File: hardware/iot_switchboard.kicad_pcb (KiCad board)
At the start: 2 copper layers, 14 parts, among them IC1 ATTINY44A-SS, P1 CONN_01X05, P2 AVR_ISP

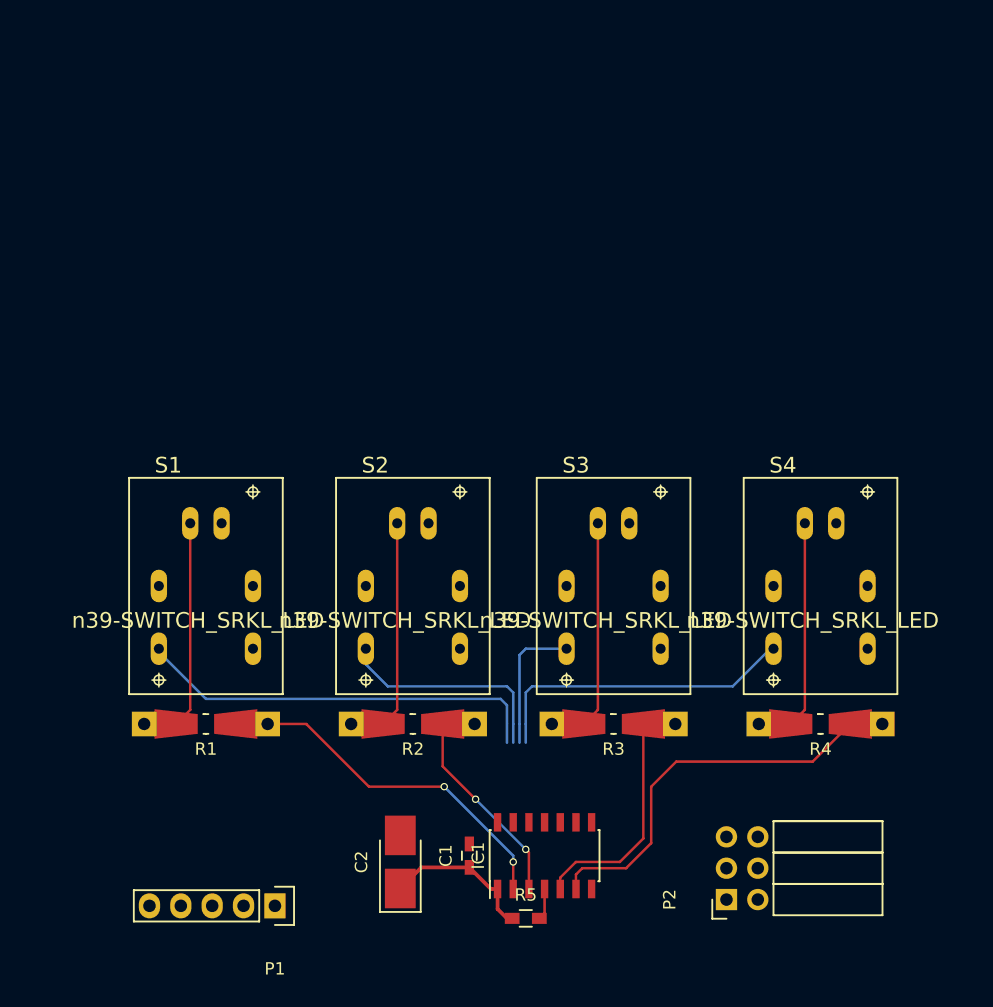
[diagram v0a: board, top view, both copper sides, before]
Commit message: layout and attiny in QFN20
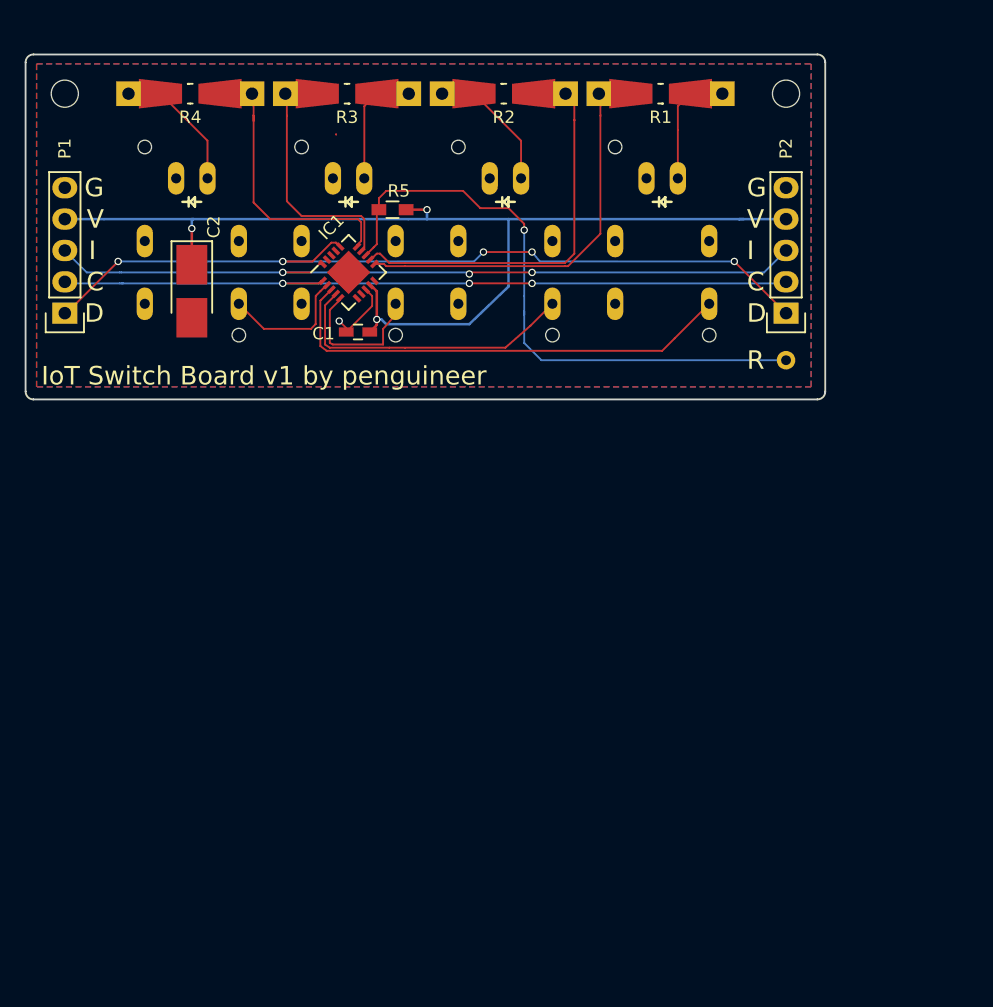
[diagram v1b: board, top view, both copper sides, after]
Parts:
- added REF**: MountingHole_2.2mm_M2_ISO14580, Mounting_Holes:MountingHole_2.2mm_M2_ISO14580, F.Cu at (163.3, 54.6)
- added REF**: MountingHole_2.2mm_M2_ISO14580, Mounting_Holes:MountingHole_2.2mm_M2_ISO14580, F.Cu at (221.7, 54.6)
- added T1: CONN_01X01, Measurement_Points:Measurement_Point_Round-TH_Small, F.Cu at (221.7, 76.2)
- IC1: value ATTINY44A-SS -> ATTINY84-M; footprint Housings_SOIC:SOIC-14_3.9x8.7mm_Pitch1.27mm -> Housings_DFN_QFN:QFN-20-1EP_4x4mm_Pitch0.5mm
- P2: value AVR_ISP -> CONN_01X05; footprint Socket_Strips:Socket_Strip_Angled_2x03 -> Socket_Strips:Socket_Strip_Straight_1x05
- R5: value R -> 10K
- S1, S2, S3, S4: moved to B.Cu
- moved R4 72.2 mm to (173.5, 54.6)
- moved R1 63.0 mm to (211.6, 54.6), turned to 180 degrees
- moved R5 58.4 mm to (189.9, 64.0), turned to 180 degrees
- moved S4 58.1 mm to (173.6, 66.5), turned to 180 degrees
- moved R3 55.4 mm to (186.2, 54.6), turned to 180 degrees
- moved R2 51.6 mm to (198.9, 54.6)
- moved P1 50.9 mm to (163.3, 72.4), turned to 90 degrees
- moved IC1 49.8 mm to (186.3, 69.1), turned to 45 degrees
- moved C2 49.2 mm to (173.6, 70.6), turned to 270 degrees
- moved P2 47.7 mm to (221.7, 72.4)
- moved S1 46.3 mm to (211.7, 66.5), turned to 180 degrees
- moved C1 43.4 mm to (187.1, 73.9), turned to 180 degrees
- moved S3 35.2 mm to (186.3, 66.5), turned to 180 degrees
- moved S2 28.9 mm to (199.0, 66.5), turned to 180 degrees
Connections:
- IC1 pad 1: VCC_IN -> SCL
- IC1 pad 10: SW4 -> (no net)
- IC1 pad 11: SW3 -> LED1
- IC1 pad 12: SW2 -> LED2
- IC1 pad 13: SW1 -> RST
- IC1 pad 14: GND -> LED3
- IC1 pad 2: LED1 -> SW4
- IC1 pad 3: LED2 -> SW1
- IC1 pad 4: RST -> SW2
- IC1 pad 5: LED3 -> SW3
- IC1 pad 6: LED4 -> (no net)
- IC1 pad 7: MOSI -> (no net)
- IC1 pad 8: INT -> GND
- IC1 pad 9: SCK -> VCC_IN
- P1 pad 1: MOSI -> SDA
- P1 pad 2: SCK -> SCL
- P2 pad 1: INT -> SDA
- P2 pad 2: VCC_IN -> SCL
- P2 pad 3: SCK -> INT
- P2 pad 4: MOSI -> VCC_IN
- P2 pad 5: RST -> GND
- S1 pad 4: (no net) -> GND
- S2 pad 4: (no net) -> GND
- S3 pad 4: (no net) -> GND
- S4 pad 4: (no net) -> GND
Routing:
- net VCC_IN: track 12.4 -> 87.1 mm, vias 0 -> 3
- net SDA: track 0.00 -> 68.0 mm, vias 0 -> 5
- net INT: track 0.00 -> 63.8 mm, vias 0 -> 3
- net SCL: track 0.00 -> 62.2 mm, vias 0 -> 3
- net RST: track 2.56 -> 49.9 mm, vias 0 -> 1
- net SW4: track 25.6 -> 10.8 mm
- net LED2: track 18.8 -> 33.3 mm, vias 2 -> 0
- net LED4: track 35.7 -> 23.4 mm
- net Net-(R3-Pad1): track 19.3 -> 9.87 mm
- net Net-(R1-Pad1): track 19.3 -> 9.87 mm
- net Net-(R2-Pad1): track 19.3 -> 11.0 mm
- net Net-(R4-Pad1): track 19.3 -> 11.0 mm
- net GND: track 0.00 -> 5.64 mm, vias 0 -> 1
- net SW2: track 19.0 -> 24.6 mm
- net SW1: track 33.6 -> 38.2 mm
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- added copper zone on B.Cu, net GND
- added copper zone on F.Cu, net GND
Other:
- board outline added: 64.8 x 27.9 mm
- net class DATA: clearance 0.2 -> 0.09906; trace_width 0.2032 -> 0.1524
- net class Default: clearance 0.2 -> 0.1016; trace_width 0.25 -> 0.1524
- net class PWR: clearance 0.2 -> 0.1016; trace_width 0.3048 -> 0.2032
- rule trace_clearance: 0.2 -> 0.1016
- rule trace_min: 0.2 -> 0.1
- rule via_min_drill: 0.3 -> 0.2
- rule via_min_size: 0.4 -> 0.3
- board text added: "C"
- board text added: "D"
- board text added: "G"
- board text added: "I"
- board text added: "IoT Switch Board v1 by penguineer"
- board text added: "R"
- board text added: "V"

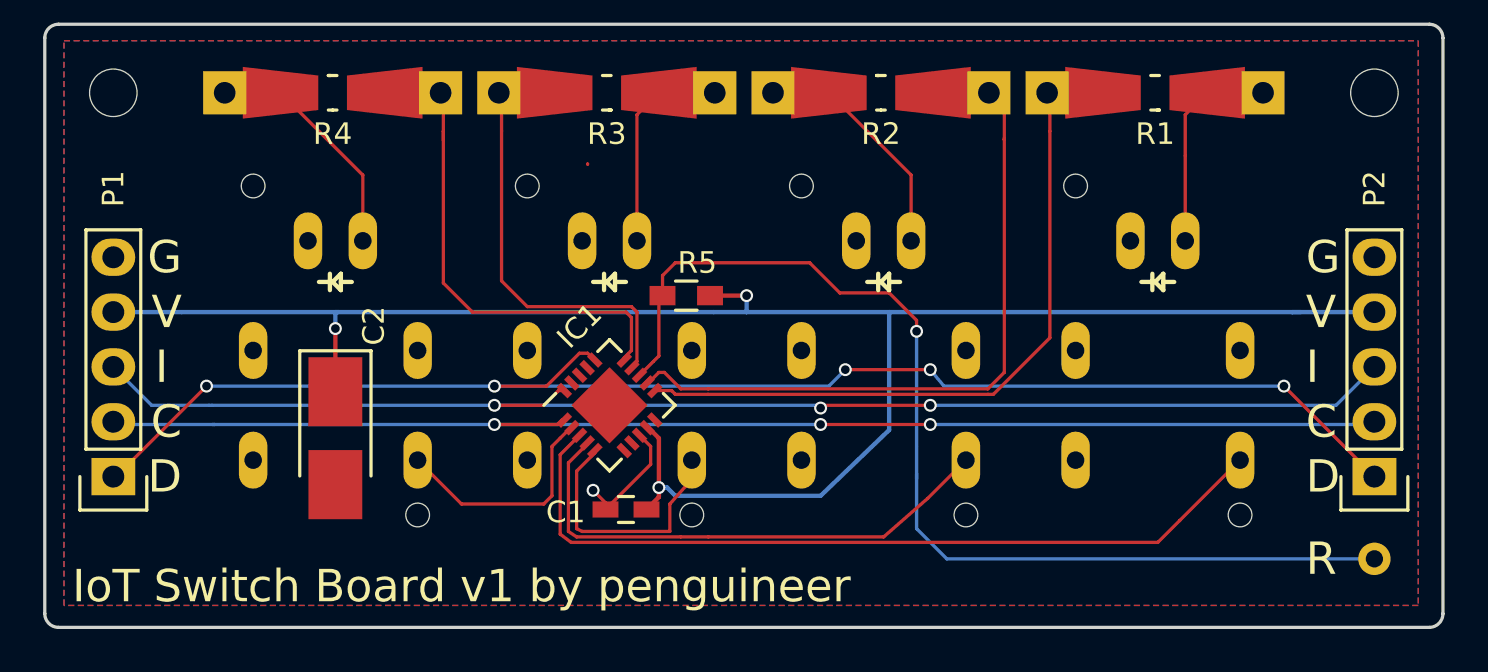
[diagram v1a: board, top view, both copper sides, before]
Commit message: Adapt to Oshpark design rules
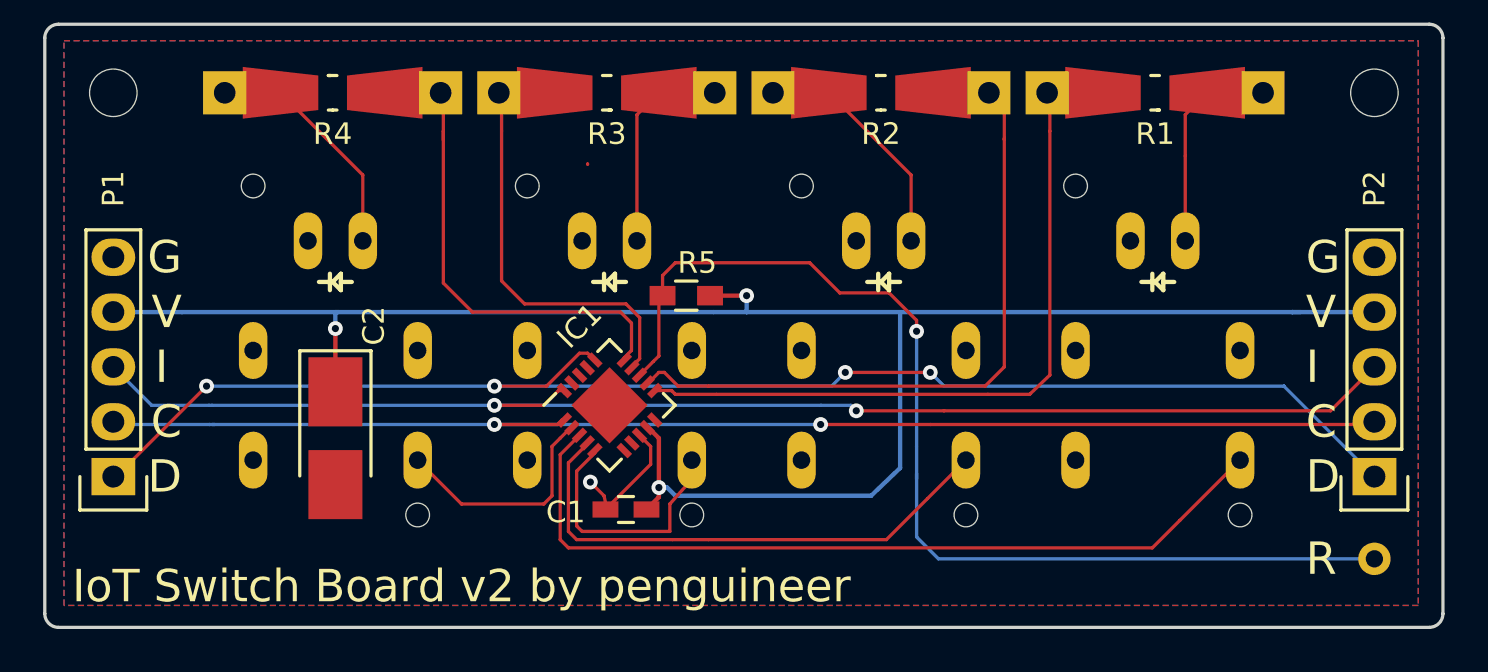
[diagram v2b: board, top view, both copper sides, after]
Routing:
- net VCC_IN: track 87.1 -> 88.7 mm
- net LED1: track 33.2 -> 34.2 mm
- net SCL: track 62.2 -> 62.3 mm, vias 3 -> 2
- net SDA: track 68.0 -> 67.8 mm, vias 5 -> 4
- net INT: track 63.8 -> 63.7 mm, vias 3 -> 2
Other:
- net class DATA: clearance 0.09906 -> 0.1524; via_dia 0.6 -> 0.6858; via_drill 0.4 -> 0.3302
- net class Default: clearance 0.1016 -> 0.1524; via_dia 0.6 -> 0.6858; via_drill 0.4 -> 0.3302
- net class PWR: clearance 0.1016 -> 0.1524; via_dia 0.6 -> 0.6858; via_drill 0.4 -> 0.3302
- rule trace_clearance: 0.1016 -> 0.1524
- rule trace_min: 0.1 -> 0.1524
- rule via_min_drill: 0.2 -> 0.3302
- rule via_min_size: 0.3 -> 0.6858
- board text added: "IoT Switch Board v2 by penguineer"
- board text removed: "IoT Switch Board v1 by penguineer"
